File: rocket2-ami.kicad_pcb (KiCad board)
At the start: 2 copper layers, 54 x 54 mm, 52 parts, among them J1 ARM Cortex Debug, J3 XT60 POWER, U1 STM32F105RCT6, U2 LD1086DT33TR, U4 USBLC6-2SC6, U5 ADXL383, Y1 8MHz

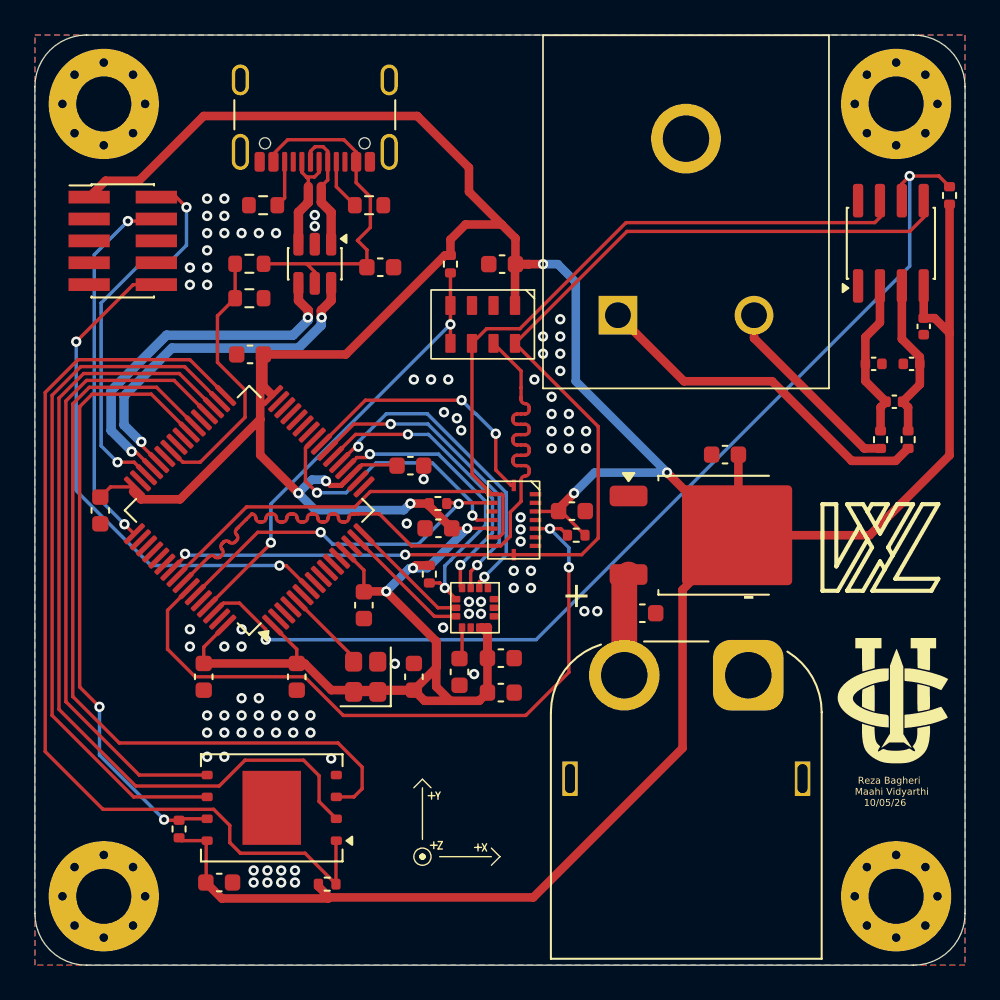
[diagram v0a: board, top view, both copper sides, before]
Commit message: Switched to buck convertor!
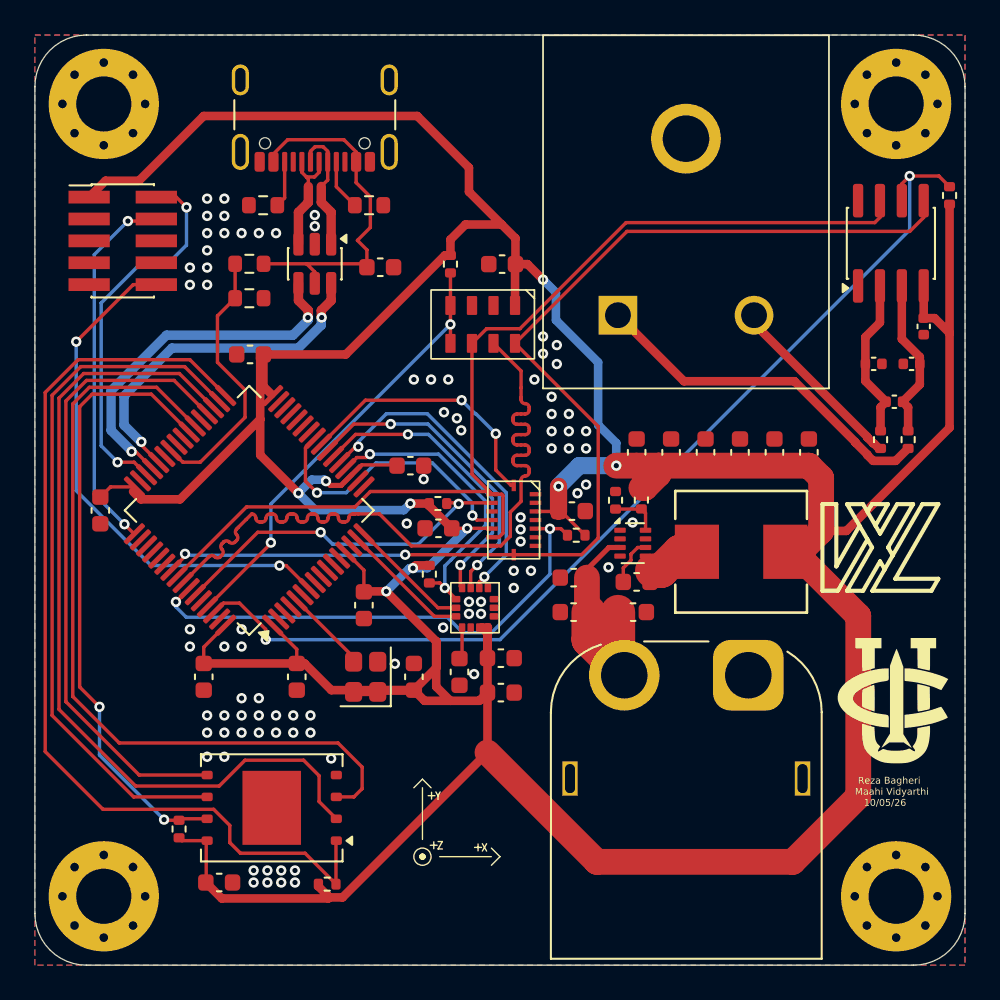
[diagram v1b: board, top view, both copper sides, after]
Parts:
- removed C1, C2: 10uF, Capacitor_SMD:C_0603_1608Metric
- removed U2: LD1086DT33TR, Package_TO_SOT_SMD:TO-252-2
- added C15: 10uF, Capacitor_SMD:C_0603_1608Metric, F.Cu at (129.3, 129.5)
- added C17: 100nF, Capacitor_SMD:C_0603_1608Metric, F.Cu at (129.3, 131.5)
- added C19: 10uF, Capacitor_SMD:C_0603_1608Metric, F.Cu at (132.7, 131.5)
- added C20: 100nF, Capacitor_SMD:C_0603_1608Metric, F.Cu at (132.9, 129.8)
- added C22: 22uF, Capacitor_SMD:C_0603_1608Metric, F.Cu at (142.9, 122.2)
- added C23: 22uF, Capacitor_SMD:C_0603_1608Metric, F.Cu at (140.9, 122.2)
- added C24: 100nF, Capacitor_SMD:C_0603_1608Metric, F.Cu at (138.9, 122.2)
- added C25: 22uF, Capacitor_SMD:C_0603_1608Metric, F.Cu at (136.9, 122.2)
- added C26: 22uF, Capacitor_SMD:C_0603_1608Metric, F.Cu at (134.9, 122.2)
- added C27: 22uF, Capacitor_SMD:C_0603_1608Metric, F.Cu at (132.9, 122.2)
- added L1: 4.7 uH, 0UCIRP-KiCAD-Lib:Inductor (4.7uH) IND_03-4R7-R_EAT, F.Cu at (139.0, 128.0)
- added R8: 31.3K, Resistor_SMD:R_0402_1005Metric, F.Cu at (133.2, 125.0)
- added R9: 10K, Resistor_SMD:R_0402_1005Metric, F.Cu at (131.7, 125.0)
- added U8: TPS62933P, Package_TO_SOT_SMD:SOT-583-8, F.Cu at (132.7, 127.5)
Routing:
- net +3.3V: track 271.7 -> 290.2 mm
- net /IMU_GYRO_~{CS}: track 40.8 -> 29.8 mm
- net VCC: track 5.95 -> 13.3 mm
- net Net-(U8-SW): track 0.00 -> 3.05 mm
- net Net-(U8-FB): track 0.00 -> 2.84 mm
- net Net-(U8-BST): track 0.00 -> 2.80 mm
- net /TC_~{CS}: track 60.3 -> 59.0 mm
- net GND: vias 88 -> 87

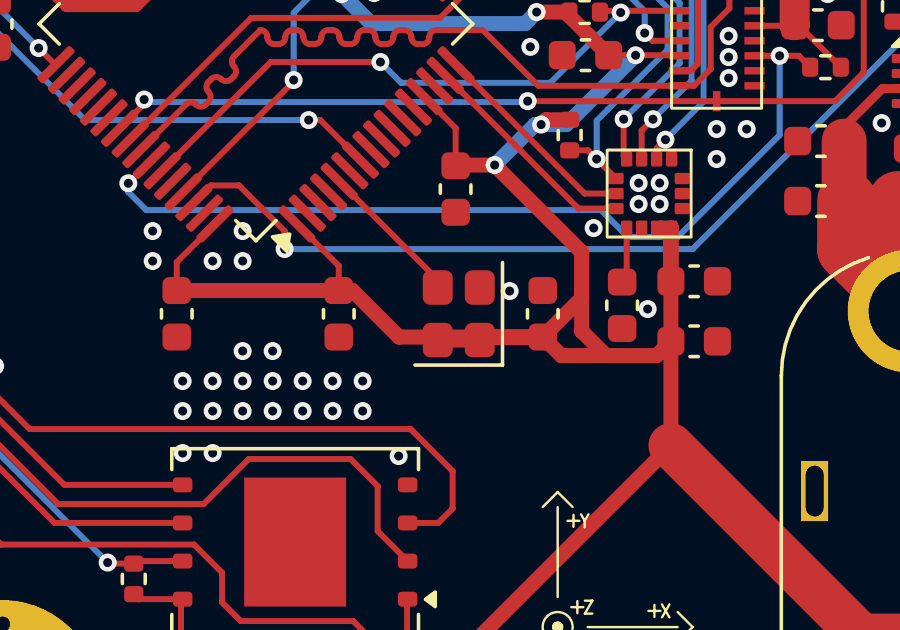
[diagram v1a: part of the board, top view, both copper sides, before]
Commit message: Upgraded to 16 mhz clock (same as our other boards)
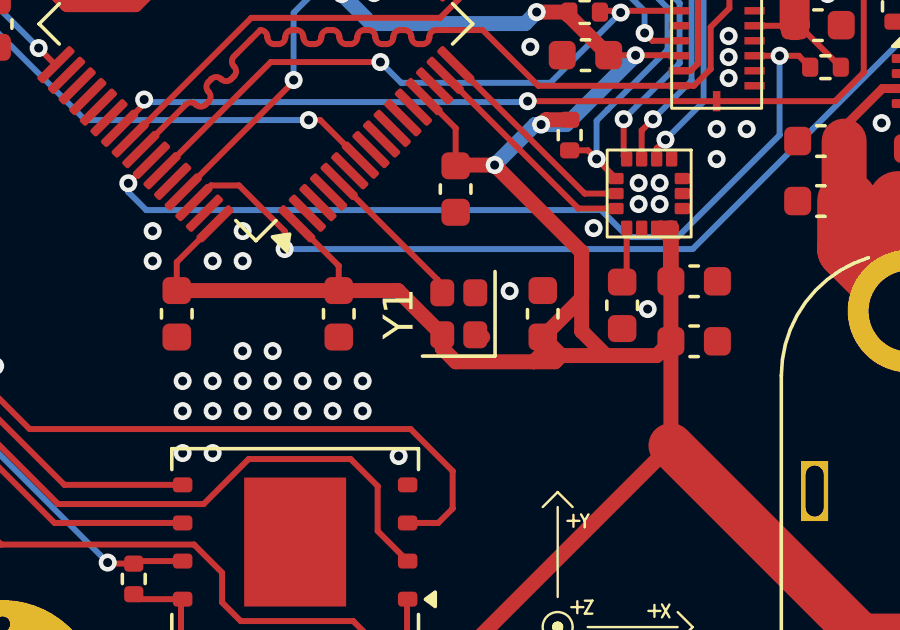
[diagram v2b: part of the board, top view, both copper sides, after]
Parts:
- Y1: value 8MHz -> 16MHz; footprint Crystal:Crystal_SMD_2520-4Pin_2.5x2.0mm -> Crystal:Crystal_SMD_2016-4Pin_2.0x1.6mm
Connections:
- Y1 pad 1: +3.3V -> unconnected-(Y1-Pad1)
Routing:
- net +3.3V: track 290.2 -> 289.0 mm

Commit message: Updated schematic & layout to remove all ERC & DRC errors & all ERC warnings
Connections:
- U6 pad 1: /IMU_INT2 -> unconnected-(U6-INT2-Pad1)
- U6 pad 13: /IMU_INT4 -> unconnected-(U6-INT4-Pad13)
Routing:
- net GND: vias 87 -> 94

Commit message: Added LED and UART
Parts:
- added C1: 4.7uF, Capacitor_SMD:C_0603_1608Metric, F.Cu at (113.8, 116.5)
- added C2: 100nF, Capacitor_SMD:C_0603_1608Metric, F.Cu at (103.9, 131.7)
- added D1: LED_ARGB, 0UCIRP-KiCAD-Lib:LED RGB (0606) APTF1616LSEEZGKQBKC, F.Cu at (118.2, 115.3)
- added J4: Conn_01x04_Pin, Connector_PinHeader_2.54mm:PinHeader_1x04_P2.54mm_Vertical, F.Cu at (117.0, 149.9)
- added R10: 10K, Resistor_SMD:R_0603_1608Metric, F.Cu at (105.9, 133.6)
- added R11: 325, Resistor_SMD:R_0402_1005Metric, F.Cu at (115.2, 119.1)
- added R12: 325, Resistor_SMD:R_0402_1005Metric, F.Cu at (117.2, 118.1)
- added R17: 750, Resistor_SMD:R_0402_1005Metric, F.Cu at (114.3, 118.3)
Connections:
- U1 pad 27: unconnected-(U1-PB1-Pad27) -> /LED_B
- U1 pad 29: unconnected-(U1-PB10-Pad29) -> /LED_G
- U1 pad 30: unconnected-(U1-PB11-Pad30) -> /LED_R
- U1 pad 51: unconnected-(U1-PC10-Pad51) -> /LoRA_TX
- U1 pad 52: unconnected-(U1-PC11-Pad52) -> /LoRA_RX
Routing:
- net /LoRA_RX: track 0.00 -> 32.4 mm, vias 0 -> 1
- net /LoRA_TX: track 0.00 -> 31.0 mm, vias 0 -> 1
- net +3.3V: track 289.0 -> 298.9 mm
- net Net-(D1-GK): track 0.00 -> 5.84 mm
- net /~{RST}: track 30.6 -> 36.3 mm, vias 2 -> 3
- net Net-(D1-RK): track 0.00 -> 4.77 mm
- net /LED_B: track 0.00 -> 4.19 mm
- net /LED_G: track 0.00 -> 2.23 mm
- net Net-(D1-BK): track 0.00 -> 2.04 mm
- net /LED_R: track 0.00 -> 1.83 mm
- net /VBUS: track 20.9 -> 20.3 mm
- net GND: vias 94 -> 97
